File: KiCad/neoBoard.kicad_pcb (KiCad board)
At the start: 2 copper layers, 40 x 40 mm, 74 parts, among them J1 SW, J10 CONN_01X04_Straight, J11 CONN_01X04_Straight, J12 CONN_01X04_Straight, J13 CONN_01X04_Straight, J2 μUSB, J3 BATT, J6 CONN_01X12_Straight, J7 CONN_02X12_Straight, J8 CONN_01X04_Straight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

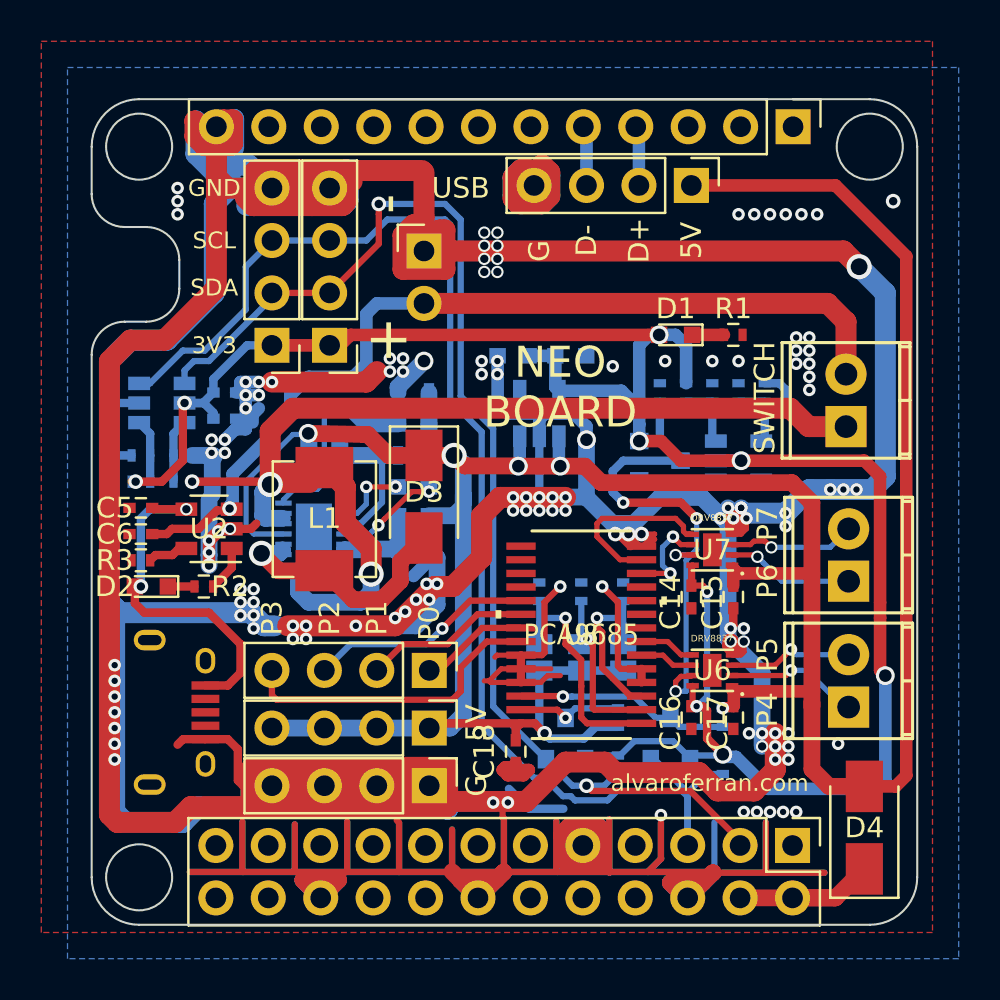
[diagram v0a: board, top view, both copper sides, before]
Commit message: Boost circuit re-routed
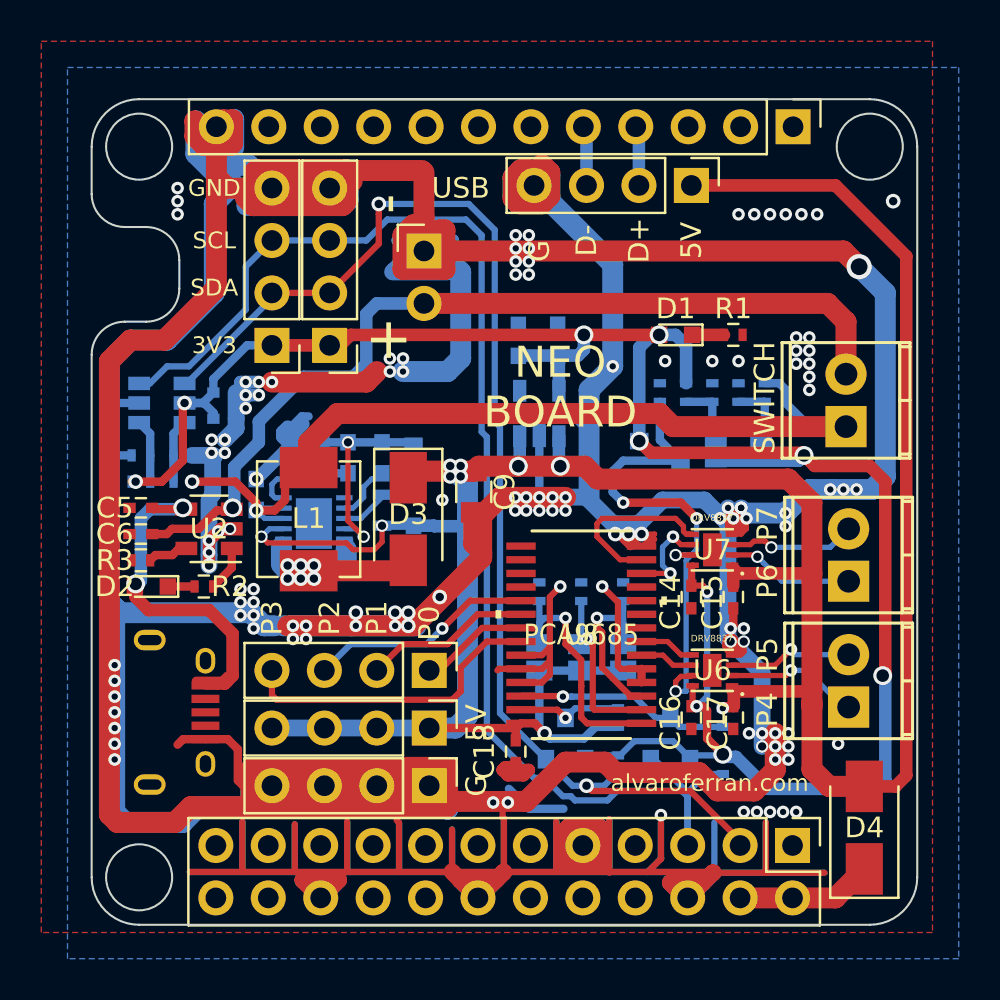
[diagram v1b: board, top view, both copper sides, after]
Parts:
- removed R16: 0, Resistors_SMD:R_0603
- C9: footprint Capacitors_SMD:C_0603 -> Capacitors_SMD:C_0805; moved to F.Cu
- moved R4 5.61 mm to (159.0, 81.7)
- moved C7 5.51 mm to (164.1, 85.0), turned to 90 degrees
- moved C8 5.05 mm to (156.5, 84.2), turned to 90 degrees
- moved C13 3.57 mm to (160.9, 82.4), turned to 90 degrees
- moved R5 3.37 mm to (162.6, 85.0), turned to 90 degrees
- moved R10 3.26 mm to (159.0, 83.2)
- moved C9 3.14 mm to (167.0, 84.1), turned to 270 degrees
- moved C12 2.08 mm to (162.6, 82.4), turned to 270 degrees
- moved D3 1.32 mm to (163.8, 85.4)
- moved C4 0.99 mm to (171.1, 76.7), turned to 90 degrees
- moved C2 0.79 mm to (169.2, 76.7), turned to 90 degrees
- moved L1 0.76 mm to (159.0, 85.4)
- moved U3 0.25 mm to (159.3, 85.6)
- moved R17 0.13 mm to (164.1, 82.4), turned to 90 degrees
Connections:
- C8 pad 2: GNDPWR -> GND
- C9 pad 2: GNDPWR -> GND
- U3 pad 5: GNDPWR -> GND
- U3 pad 6: GNDPWR -> GND
- U8 pad 15: (no net) -> Net-(U8-Pad15)
- U8 pad 16: (no net) -> Net-(U8-Pad16)
- U8 pad 17: (no net) -> Net-(U8-Pad17)
- U8 pad 18: (no net) -> Net-(U8-Pad18)
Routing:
- net GND: track 595.1 -> 619.6 mm, vias 129 -> 125
- net VBAT: track 60.2 -> 42.5 mm, vias 3 -> 2
- net GNDPWR: track 7.04 -> 0.00 mm
- net Net-(C7-Pad2): track 10.3 -> 4.81 mm
- net Net-(R10-Pad2): track 6.88 -> 2.38 mm
- net 5V: track 148.1 -> 144.8 mm, vias 6 -> 10
- net Net-(D3-Pad2): track 12.2 -> 9.63 mm, vias 1 -> 6
- net Net-(C13-Pad1): track 3.13 -> 1.15 mm
- net 3.3V: track 108.3 -> 110.0 mm, vias 9 -> 10
- net Net-(C5-Pad1): track 17.4 -> 18.7 mm
- net Net-(C12-Pad2): track 3.64 -> 2.82 mm, vias 2 -> 0
- net /SCL: track 65.8 -> 66.4 mm

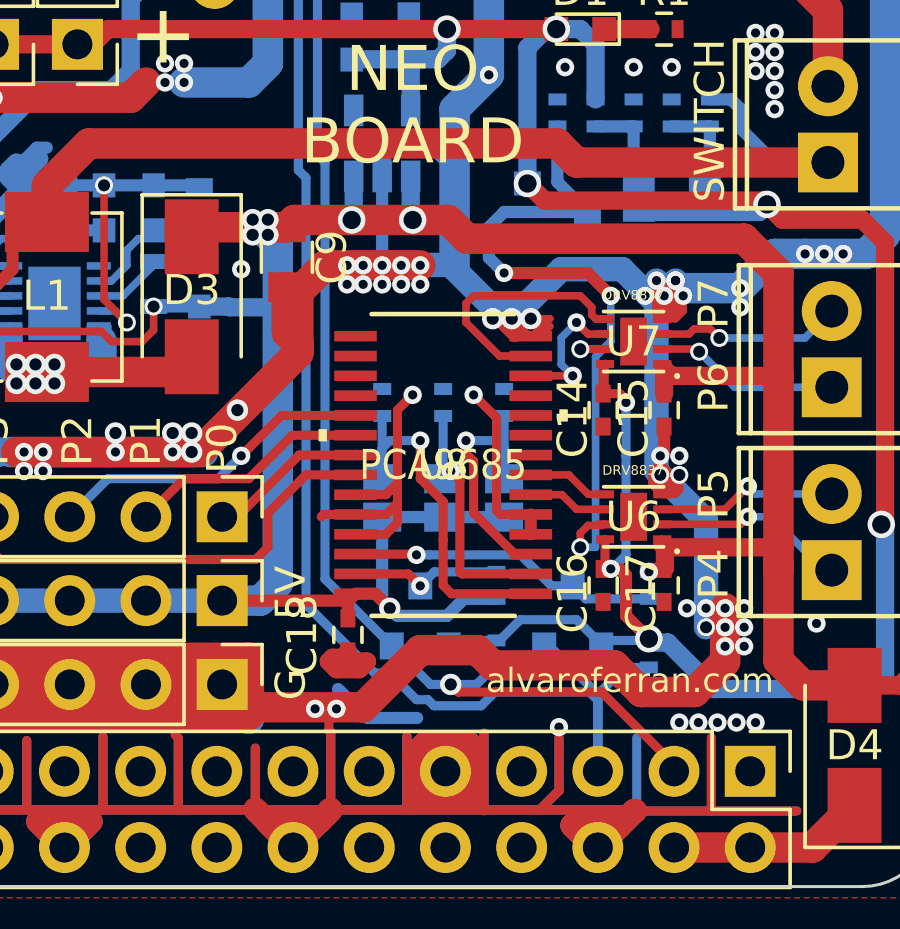
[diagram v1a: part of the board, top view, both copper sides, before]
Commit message: Silkscreen fixes
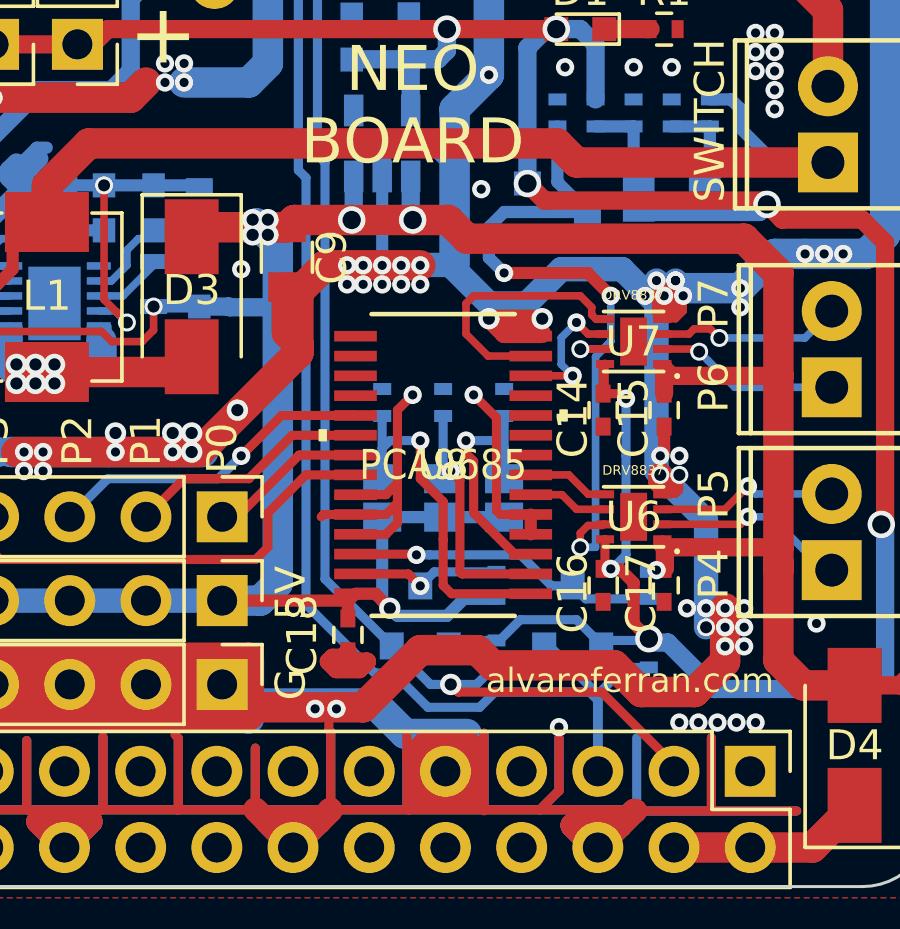
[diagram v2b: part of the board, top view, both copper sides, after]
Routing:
- net GND: track 619.6 -> 624.1 mm
- net 5V: track 144.8 -> 145.3 mm
